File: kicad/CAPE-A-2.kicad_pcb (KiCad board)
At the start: 4 copper layers, 55 x 35 mm, 40 parts, among them X2Y-CAN 4.7nF X2Y, X2Y-RS485 4.7nF X2Y

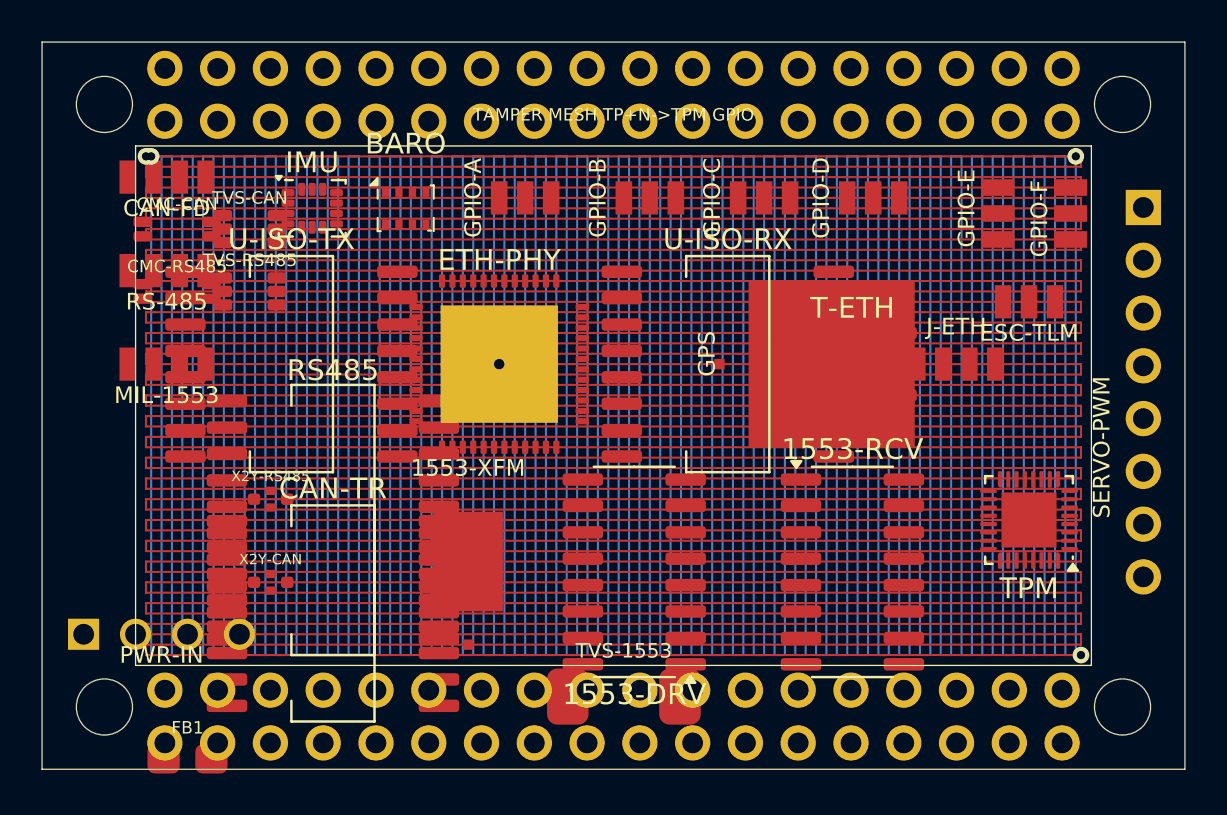
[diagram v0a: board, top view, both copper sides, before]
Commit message: updated the xcvr to fix drc issues an
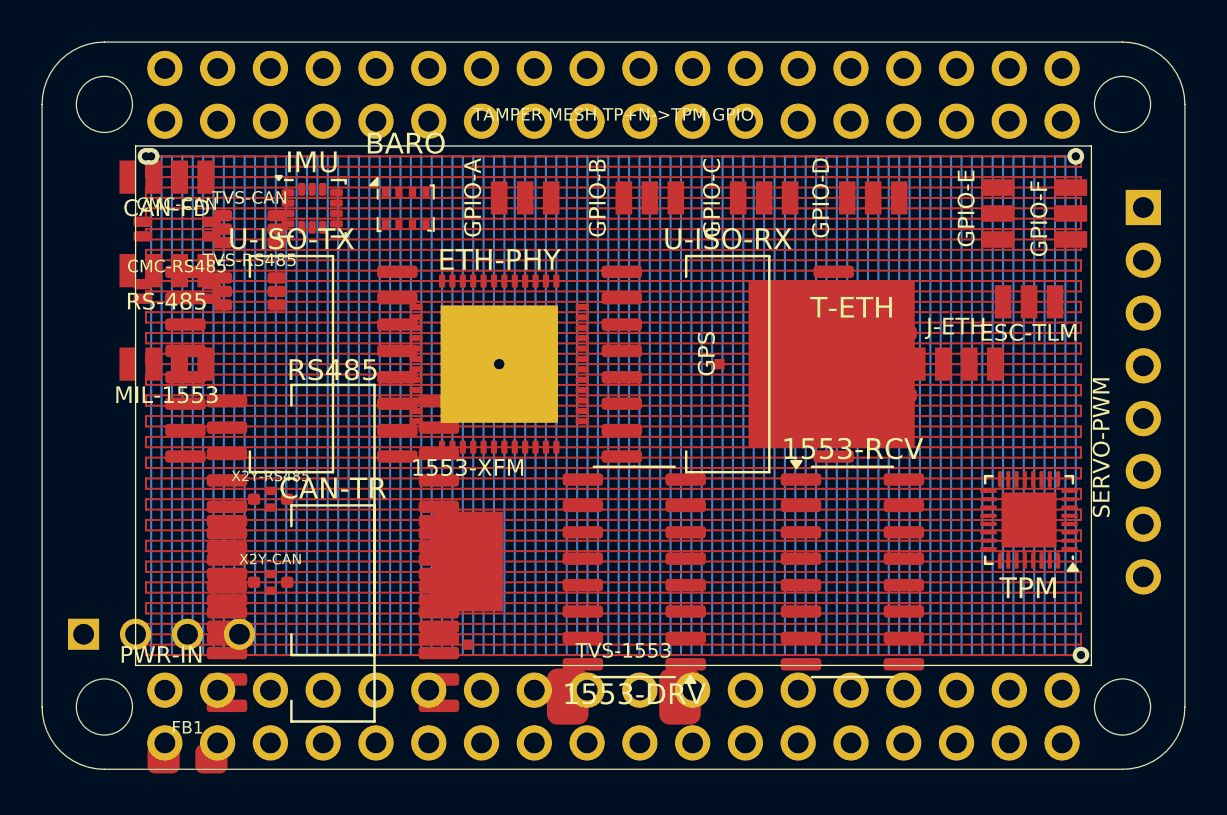
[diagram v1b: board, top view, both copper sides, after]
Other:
- outline, holes or cut-outs redrawn
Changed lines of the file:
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@@
 		(embedded_fonts no)
 	)
-	(gr_line
-		(start 121 87.5)
-		(end 176 87.5)
+	(gr_arc
+		(start 121 90.5)
+		(mid 121.87868 88.37868)
+		(end 124 87.5)
 		(stroke
 			(width 0.05)
@@
 	)
 	(gr_line
-		(start 176 122.5)
-		(end 121 122.5)
+		(start 124 87.5)
+		(end 173 87.5)
+		(stroke
+			(width 0.05)
+			(type solid)
+		)
+		(layer "Edge.Cuts")
+	)
+	(gr_arc
+		(start 173 87.5)
+		(mid 175.12132 88.37868)
+		(end 176 90.5)
 		(stroke
 			(width 0.05)
@@
 	)
 	(gr_line
-		(start 121 122.5)
-		(end 121 87.5)
+		(start 176 90.5)
+		(end 176 119.5)
+		(stroke
+			(width 0.05)
+			(type solid)
+		)
+		(layer "Edge.Cuts")
+	)
+	(gr_arc
+		(start 176 119.5)
+		(mid 175.12132 121.62132)
+		(end 173 122.5)
 		(stroke
 			(width 0.05)
@@
 	)
 	(gr_line
-		(start 176 87.5)
-		(end 176 122.5)
+		(start 173 122.5)
+		(end 124 122.5)
 		(stroke
 			(width 0.05)
+			(type solid)
+		)
+		(layer "Edge.Cuts")
+	)
+	(gr_arc
+		(start 124 122.5)
+		(mid 121.87868 121.62132)
+		(end 121 119.5)
+		(stroke
+			(width 0.05)
+			(type solid)
+		)
+		(layer "Edge.Cuts")
+	)
+	(gr_line
+		(start 121 119.5)
+		(end 121 90.5)
+		(stroke
+			(width 0.05)
